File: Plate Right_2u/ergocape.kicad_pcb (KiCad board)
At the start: 2 copper layers, 183.2 x 140.8 mm, 43 parts

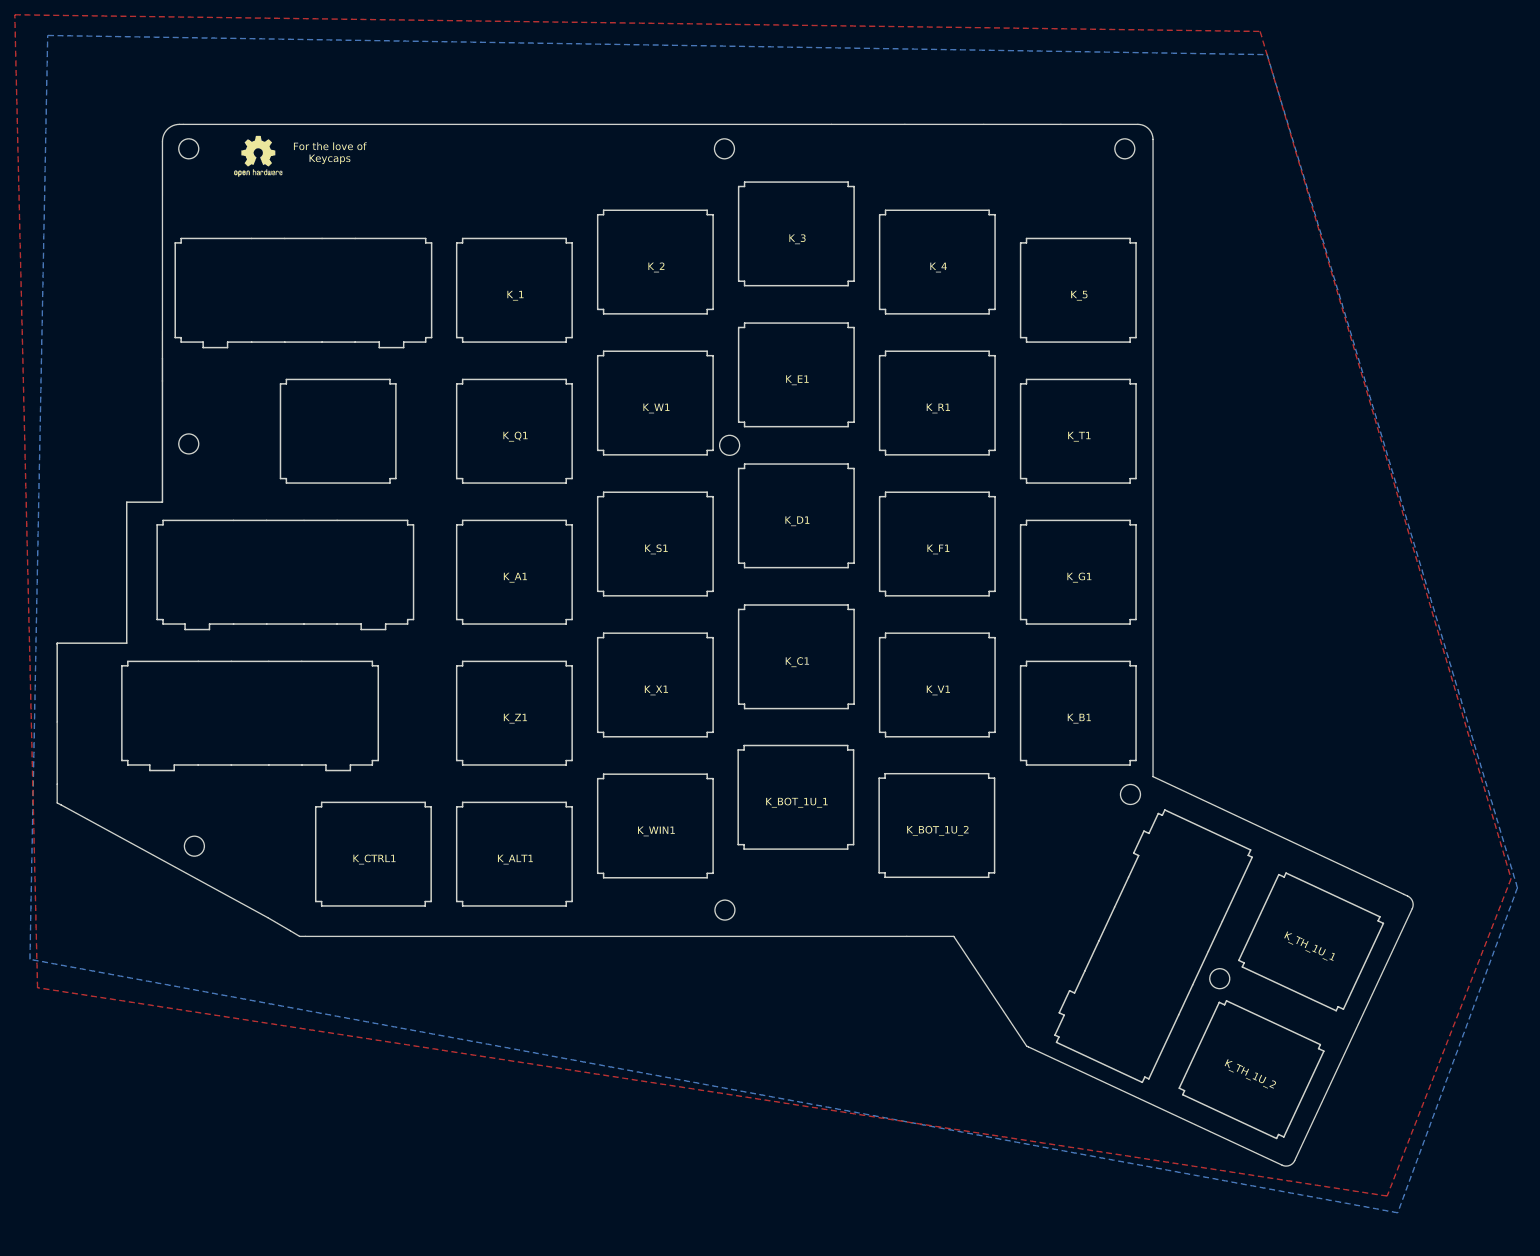
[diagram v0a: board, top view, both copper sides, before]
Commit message: fix pro micro footprint
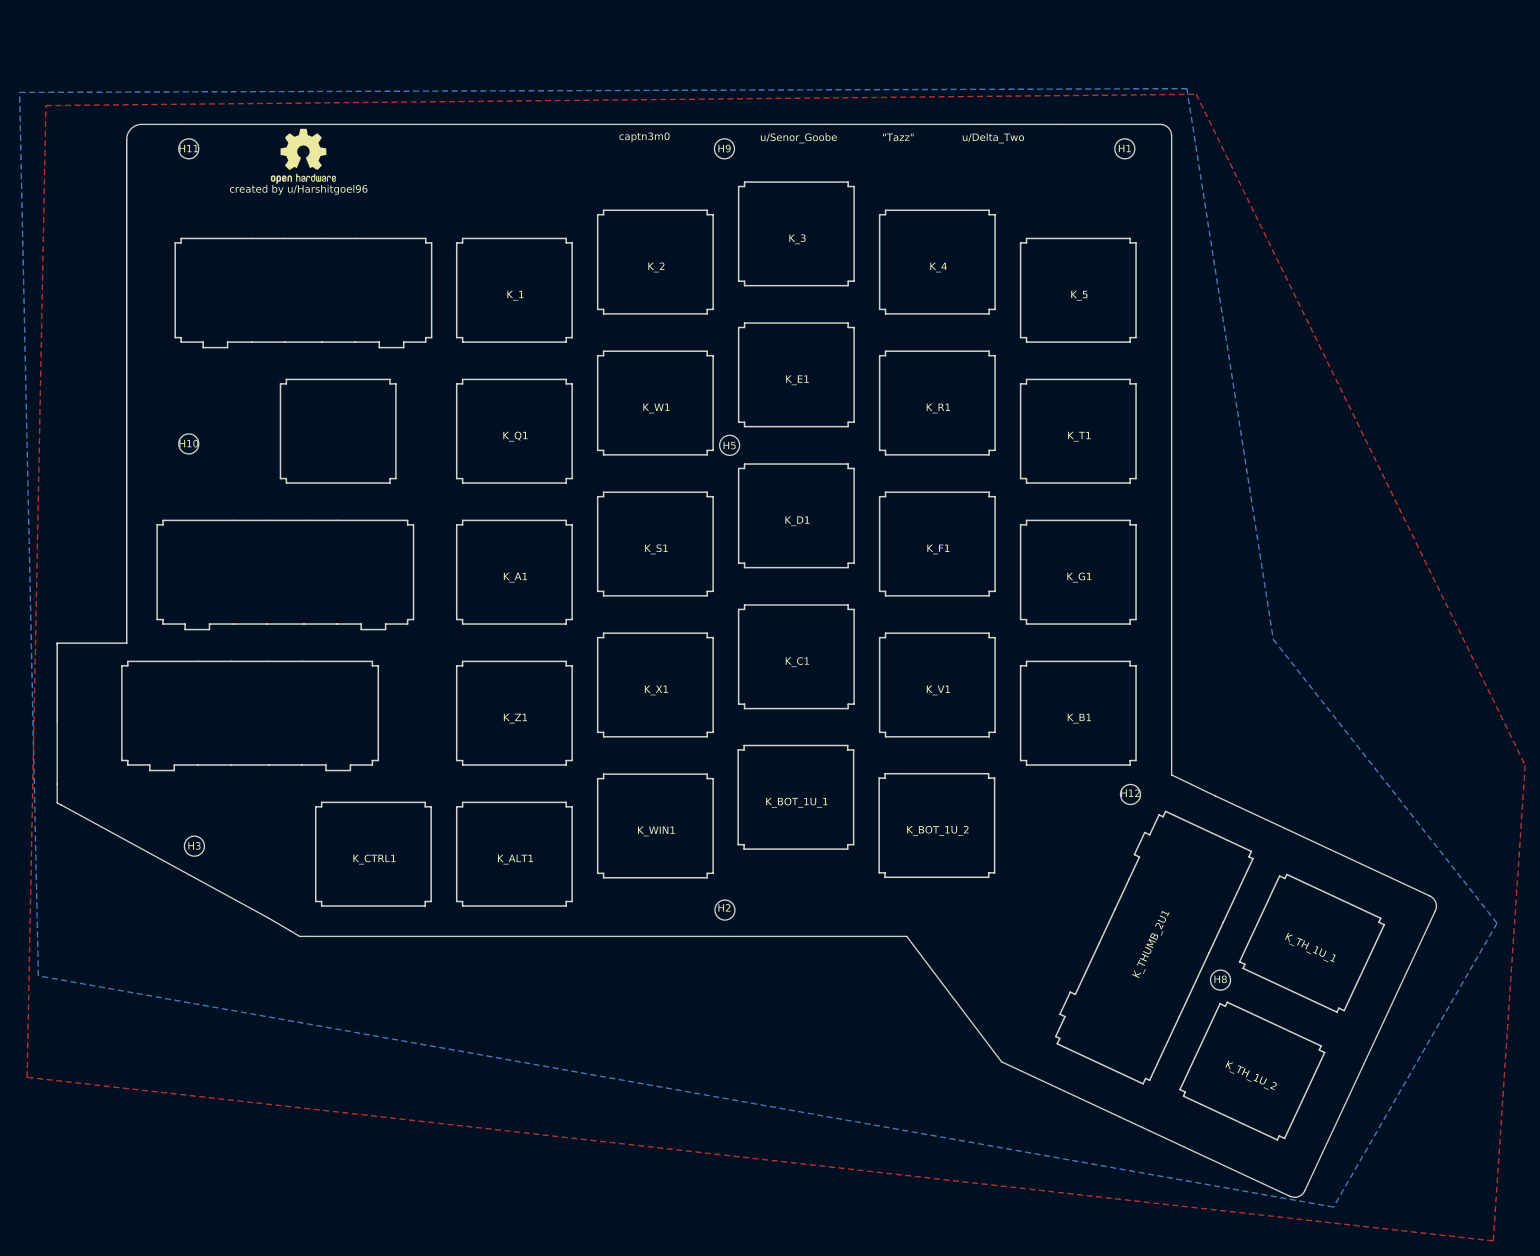
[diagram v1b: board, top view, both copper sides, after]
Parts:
- removed the REF** at (49.5, 21.6) (x2)
- added REF**: OSHW-Logo2_9.8x8mm_SilkScreen, logo_lib:OSHW-Logo2_9.8x8mm_SilkScreen, B.Cu at (55.6, 21.6)
- added REF**: OSHW-Logo2_9.8x8mm_SilkScreen, logo_lib:OSHW-Logo2_9.8x8mm_SilkScreen, F.Cu at (55.6, 21.6)
- K_BKSP_1: moved to B.Cu
- moved K_TH_1U_1 0.22 mm to (191.9, 127.9)
- moved H8 0.22 mm to (179.6, 132.9)
- moved K_THUMB_2U1 0.22 mm to (170.6, 128.5)
- moved K_TH_1U_2 0.22 mm to (183.9, 145.2)
- turned K_BKSP_1 to 180 degrees
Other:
- board size 183.2 x 140.8 mm -> 186.4 x 145 mm
- board text added: ""Tazz""
- board text added: "captn3m0"
- board text added: "created by u/Harshitgoel96"
- board text added: "u/Delta_Two"
- board text added: "u/Senor_Goobe"
- board text removed: "For the love of Keycaps"
